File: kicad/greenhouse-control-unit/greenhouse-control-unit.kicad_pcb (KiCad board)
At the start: 2 copper layers, 71 parts, among them J1 Pluggable_Terminal_01x02, J10 Molex_KK-254_01x10, J10_LittleBuck1 Conn_01x01_Female, J11_LittleBuck1 Conn_01x01_Female, J12_BigBuck1 Conn_01x01_Female, J13_BigBuck1 Conn_01x01_Female, J14_LittleBuck1 Conn_01x01_Female, J15_LittleBuck1 Conn_01x01_Female, J2 Pluggable_Terminal_01x02, J3 Pluggable_Terminal_01x02, J4 Molex_KK-254_01x08, J5 Conn_01x10_Female, J6 Conn_01x10_Female, J6_BigBuck1 Conn_01x01_Female, J7 Conn_01x15_Female, J7_BigBuck1 Conn_01x01_Female, J8 Conn_01x15_Female, J9 Molex_KK-396_01x16, Q1 2N7000, Q10 IRLB8721PBF, Q11 IRLB8721PBF, Q12 2N7000, Q13 2N7000, Q2 2N7000, Q3 2N7000, Q4 IRLB8721PBF, Q5 IRLB8721PBF, Q6 IRLB8721PBF, Q7 IRLB8721PBF, Q8 IRLB8721PBF, Q9 IRLB8721PBF, U1 74HC595, U2 74HC595

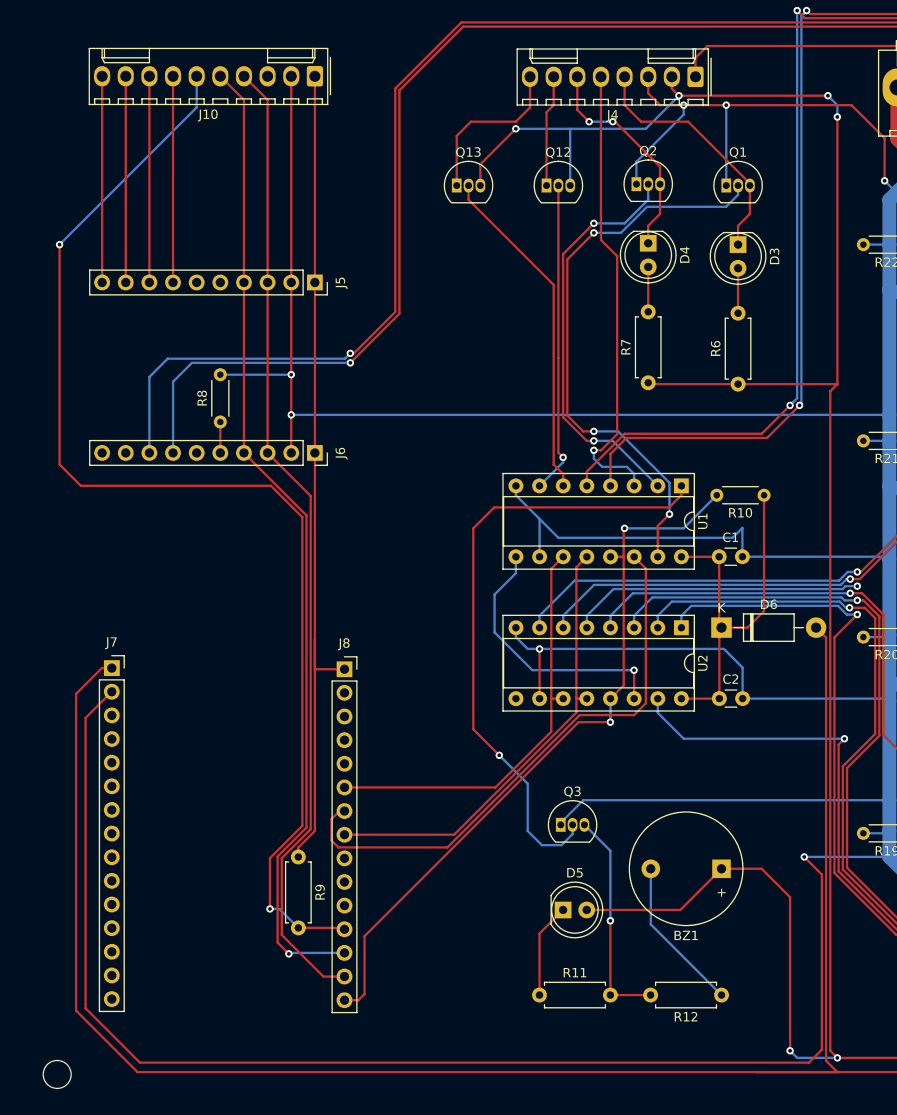
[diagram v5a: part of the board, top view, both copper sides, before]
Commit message: Tweaked PCB tracks
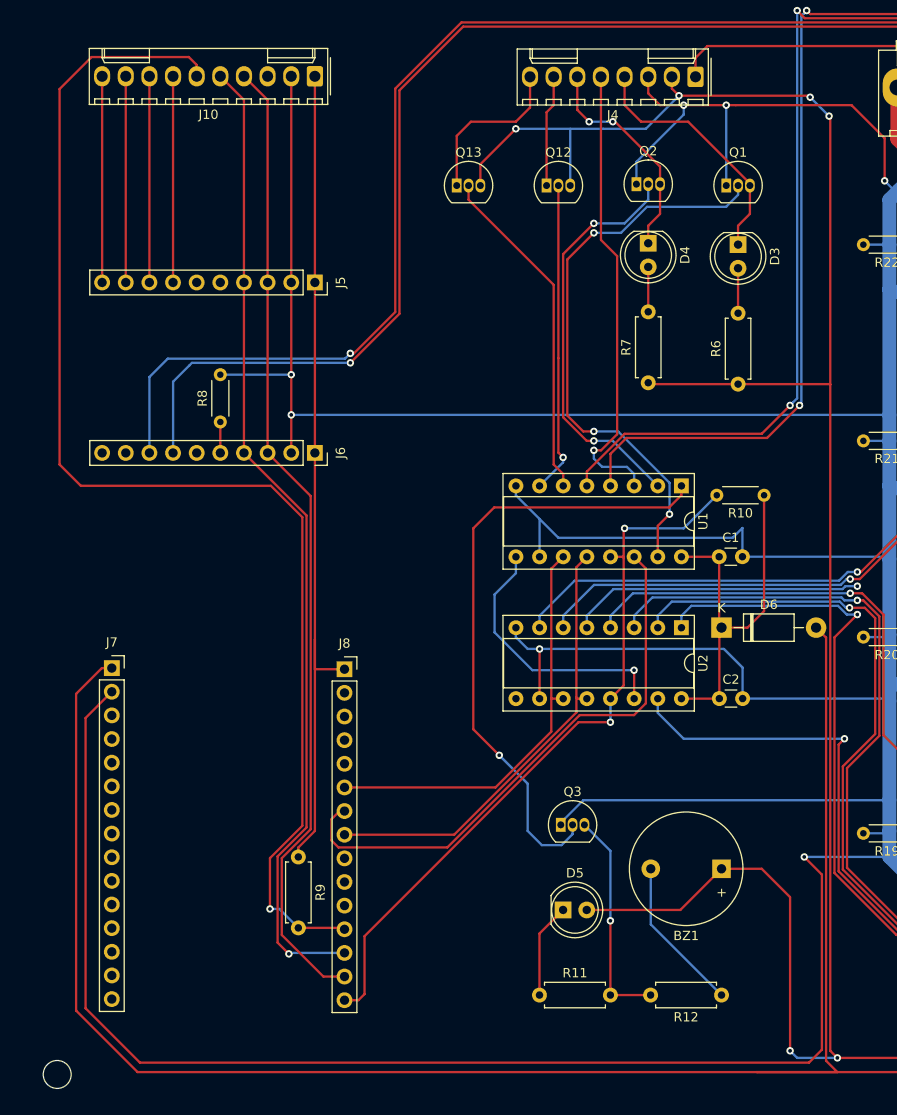
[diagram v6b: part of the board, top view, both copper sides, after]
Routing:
- net /MC_D3: track 128.7 -> 138.9 mm, vias 2 -> 1
- net +5V: track 372.0 -> 369.4 mm
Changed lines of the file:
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@@
     (fp_line (start 0.621 -0.92) (end 1.879 -0.92) (layer "F.SilkS") (width 0.12))
     (fp_line (start 0.621 0.92) (end 1.879 0.92) (layer "F.SilkS") (width 0.12))
+    (fp_line (start 3.55 1.05) (end 3.55 -1.05) (layer "F.CrtYd") (width 0.05))
     (fp_line (start -1.05 1.05) (end 3.55 1.05) (layer "F.CrtYd") (width 0.05))
     (fp_line (start -1.05 -1.05) (end -1.05 1.05) (layer "F.CrtYd") (width 0.05))
     (fp_line (start 3.55 -1.05) (end -1.05 -1.05) (layer "F.CrtYd") (width 0.05))
-    (fp_line (start 3.55 1.05) (end 3.55 -1.05) (layer "F.CrtYd") (width 0.05))
     (fp_line (start 2.75 -0.8) (end -0.25 -0.8) (layer "F.Fab") (width 0.1))
     (fp_line (start 2.75 0.8) (end 2.75 -0.8) (layer "F.Fab") (width 0.1))
@@
     (fp_line (start 5.08 0) (end 4.34 0) (layer "F.Fab") (width 0.1))
     (fp_line (start 0.74 -0.8) (end 0.74 0.8) (layer "F.Fab") (width 0.1))
+    (fp_line (start 4.34 -0.8) (end 0.74 -0.8) (layer "F.Fab") (width 0.1))
     (fp_line (start 0.74 0.8) (end 4.34 0.8) (layer "F.Fab") (width 0.1))
     (fp_line (start 4.34 0.8) (end 4.34 -0.8) (layer "F.Fab") (width 0.1))
-    (fp_line (start 4.34 -0.8) (end 0.74 -0.8) (layer "F.Fab") (width 0.1))
     (pad "1" thru_hole circle (at 0 0) (size 1.4 1.4) (drill 0.7) (layers *.Cu *.Mask)
       (net 37 "/SW0_SR_Q08") (pintype "passive"))
@@
   (segment (start 108.606642 128.872) (end 108.606642 134.84) (width 0.25) (layer "B.Cu") (net 2))
   (segment (start 108.606642 134.84) (end 116.206642 142.44) (width 0.25) (layer "B.Cu") (net 2))
-  (segment (start 127.890642 148.43) (end 127.890642 77.564) (width 0.25) (layer "F.Cu") (net 3))
-  (segment (start 128.652642 149.192) (end 127.890642 148.43) (width 0.25) (layer "F.Cu") (net 3))
-  (segment (start 127.890642 77.564) (end 128.652642 76.802) (width 0.25) (layer "F.Cu") (net 3))
+  (segment (start 125.73 45.974) (end 125.57 45.814) (width 0.25) (layer "F.Cu") (net 3))
   (segment (start 111.782642 133.296) (end 116.206642 128.872) (width 0.25) (layer "F.Cu") (net 3))
   (segment (start 90.298642 53.18) (end 94.108642 49.37) (width 0.25) (layer "F.Cu") (net 3))
   (segment (start 246.317642 110.013) (end 246.317642 103.01) (width 0.25) (layer "F.Cu") (net 3))
   (segment (start 117.984642 76.802) (end 108.480642 76.802) (width 0.25) (layer "F.Cu") (net 3))
+  (segment (start 127.890642 148.43) (end 128.652642 149.192) (width 0.25) (layer "F.Cu") (net 3))
   (segment (start 128.652642 149.192) (end 221.362642 149.192) (width 0.25) (layer "F.Cu") (net 3))
-  (segment (start 128.652642 76.802) (end 128.652642 48.1) (width 0.25) (layer "F.Cu") (net 3))
+  (segment (start 127.762 48.006) (end 127.890642 48.134642) (width 0.25) (layer "F.Cu") (net 3))
   (segment (start 221.362642 149.192) (end 226.188642 144.366) (width 0.25) (layer "F.Cu") (net 3))
   (segment (start 123.572642 131.92) (end 120.524642 128.872) (width 0.25) (layer "F.Cu") (net 3))
@@
   (segment (start 120.524642 128.872) (end 116.206642 128.872) (width 0.25) (layer "F.Cu") (net 3))
   (segment (start 226.188642 144.366) (end 226.188642 130.142) (width 0.25) (layer "F.Cu") (net 3))
+  (segment (start 117.984642 76.802) (end 127.856 76.802) (width 0.25) (layer "F.Cu") (net 3))
   (segment (start 110.872642 45.052) (end 110.872642 43.782) (width 0.25) (layer "F.Cu") (net 3))
+  (segment (start 125.57 45.814) (end 111.634642 45.814) (width 0.25) (layer "F.Cu") (net 3))
+  (segment (start 127.890642 48.134642) (end 127.890642 76.836642) (width 0.25) (layer "F.Cu") (net 3))
   (segment (start 226.188642 130.142) (end 246.317642 110.013) (width 0.25) (layer "F.Cu") (net 3))
+  (segment (start 127.856 76.802) (end 127.890642 76.836642) (width 0.25) (layer "F.Cu") (net 3))
   (segment (start 101.723642 133.296) (end 111.782642 133.296) (width 0.25) (layer "F.Cu") (net 3))
-  (segment (start 117.984642 76.802) (end 128.652642 76.802) (width 0.25) (layer "F.Cu") (net 3))
+  (segment (start 127.890642 76.836642) (end 127.890642 148.43) (width 0.25) (layer "F.Cu") (net 3))
   (segment (start 111.634642 45.814) (end 110.872642 45.052) (width 0.25) (layer "F.Cu") (net 3))
   (segment (start 90.298642 55.466) (end 90.298642 53.18) (width 0.25) (layer "F.Cu") (net 3))
   (segment (start 108.480642 76.802) (end 108.332642 76.654) (width 0.25) (layer "F.Cu") (net 3))
-  (segment (start 127.636642 45.814) (end 111.634642 45.814) (width 0.25) (layer "F.Cu") (net 3))
   (via (at 128.652642 149.192) (size 0.8) (drill 0.4) (layers "F.Cu" "B.Cu") (net 3))
   (via (at 123.572642 148.43) (size 0.8) (drill 0.4) (layers "F.Cu" "B.Cu") (net 3))
-  (via (at 127.636642 45.814) (size 0.8) (drill 0.4) (layers "F.Cu" "B.Cu") (net 3))
-  (via (at 128.652642 48.1) (size 0.8) (drill 0.4) (layers "F.Cu" "B.Cu") (net 3))
+  (via (at 125.73 45.974) (size 0.8) (drill 0.4) (layers "F.Cu" "B.Cu") (net 3))
+  (via (at 127.762 48.006) (size 0.8) (drill 0.4) (layers "F.Cu" "B.Cu") (net 3))
   (via (at 111.634642 45.814) (size 0.8) (drill 0.4) (layers "F.Cu" "B.Cu") (net 3))
   (via (at 94.108642 49.37) (size 0.8) (drill 0.4) (layers "F.Cu" "B.Cu") (net 3))
-  (segment (start 128.652642 46.83) (end 127.636642 45.814) (width 0.25) (layer "B.Cu") (net 3))
   (segment (start 103.506642 49.37) (end 108.078642 49.37) (width 0.25) (layer "B.Cu") (net 3))
   (segment (start 99.950642 49.37) (end 99.950642 55.466) (width 0.25) (layer "B.Cu") (net 3))
@@
   (segment (start 103.506642 49.37) (end 94.108642 49.37) (width 0.25) (layer "B.Cu") (net 3))
   (segment (start 124.334642 149.192) (end 128.652642 149.192) (width 0.25) (layer "B.Cu") (net 3))
-  (segment (start 128.652642 48.1) (end 128.652642 46.83) (width 0.25) (layer "B.Cu") (net 3))
+  (segment (start 125.73 45.974) (end 127.762 48.006) (width 0.25) (layer "B.Cu") (net 3))
   (segment (start 120.016642 150.716) (end 224.791642 150.716) (width 0.25) (layer "F.Cu") (net 4))
   (segment (start 127.441122 149.50448) (end 127.441122 104.03848) (width 0.25) (layer "F.Cu") (net 4))
@@
   (segment (start 74.296642 123.5525) (end 74.296642 125.824) (width 0.25) (layer "F.Cu") (net 46))
   (segment (start 75.699642 122.672) (end 75.177142 122.672) (width 0.25) (layer "F.Cu") (net 46))
-  (segment (start 71.170082 124.249406) (end 71.170082 91.100158) (width 0.25) (layer "F.Cu") (net 47))
+  (segment (start 58.973321 41.656) (end 59.818642 42.501321) (width 0.25) (layer "F.Cu") (net 47))
   (segment (start 67.793924 87.724) (end 47.372642 87.724) (width 0.25) (layer "F.Cu") (net 47))
-  (segment (start 47.372642 87.724) (end 45.086642 85.438) (width 0.25) (layer "F.Cu") (net 47))
+  (segment (start 71.170082 91.100158) (end 67.793924 87.724) (width 0.25) (layer "F.Cu") (net 47))
   (segment (start 67.692642 133.19) (end 67.692642 127.726846) (width 0.25) (layer "F.Cu") (net 47))
+  (segment (start 45.086642 45.098526) (end 48.529168 41.656) (width 0.25) (layer "F.Cu") (net 47))
   (segment (start 67.692642 127.726846) (end 71.170082 124.249406) (width 0.25) (layer "F.Cu") (net 47))
+  (segment (start 47.372642 87.724) (end 45.086642 85.438) (width 0.25) (layer "F.Cu") (net 47))
+  (segment (start 45.086642 85.438) (end 45.086642 45.098526) (width 0.25) (layer "F.Cu") (net 47))
   (segment (start 75.549642 135.222) (end 75.699642 135.372) (width 0.25) (layer "F.Cu") (net 47))
-  (segment (start 71.170082 91.100158) (end 67.793924 87.724) (width 0.25) (layer "F.Cu") (net 47))
-  (segment (start 45.086642 85.438) (end 45.086642 61.816) (width 0.25) (layer "F.Cu") (net 47))
+  (segment (start 59.818642 42.501321) (end 59.818642 43.726) (width 0.25) (layer "F.Cu") (net 47))
+  (segment (start 48.529168 41.656) (end 58.973321 41.656) (width 0.25) (layer "F.Cu") (net 47))
+  (segment (start 71.170082 124.249406) (end 71.170082 91.100158) (width 0.25) (layer "F.Cu") (net 47))
   (segment (start 70.740642 135.222) (end 75.549642 135.222) (width 0.25) (layer "F.Cu") (net 47))
-  (via (at 45.086642 61.816) (size 0.8) (drill 0.4) (layers "F.Cu" "B.Cu") (net 47))
   (via (at 67.692642 133.19) (size 0.8) (drill 0.4) (layers "F.Cu" "B.Cu") (net 47))
   (segment (start 68.708642 133.19) (end 70.740642 135.222) (width 0.25) (layer "B.Cu") (net 47))
-  (segment (start 59.818642 47.084) (end 59.818642 43.726) (width 0.25) (layer "B.Cu") (net 47))
-  (segment (start 45.086642 61.816) (end 59.818642 47.084) (width 0.25) (layer "B.Cu") (net 47))
   (segment (start 67.692642 133.19) (end 68.708642 133.19) (width 0.25) (layer "B.Cu") (net 47))
   (segment (start 62.358642 84.193) (end 62.358642 80.866) (width 0.25) (layer "F.Cu") (net 48))

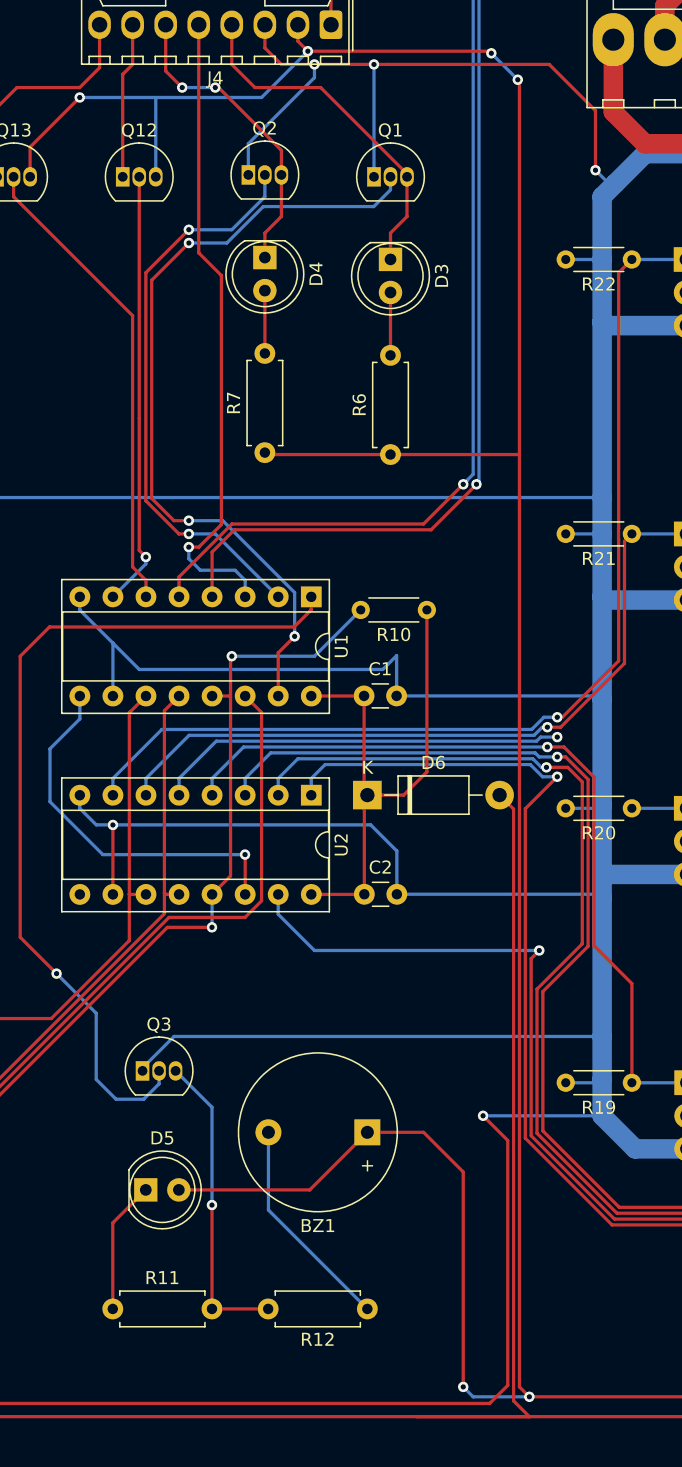
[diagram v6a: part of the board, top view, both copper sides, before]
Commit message: Tweaked PCB tracks (more)
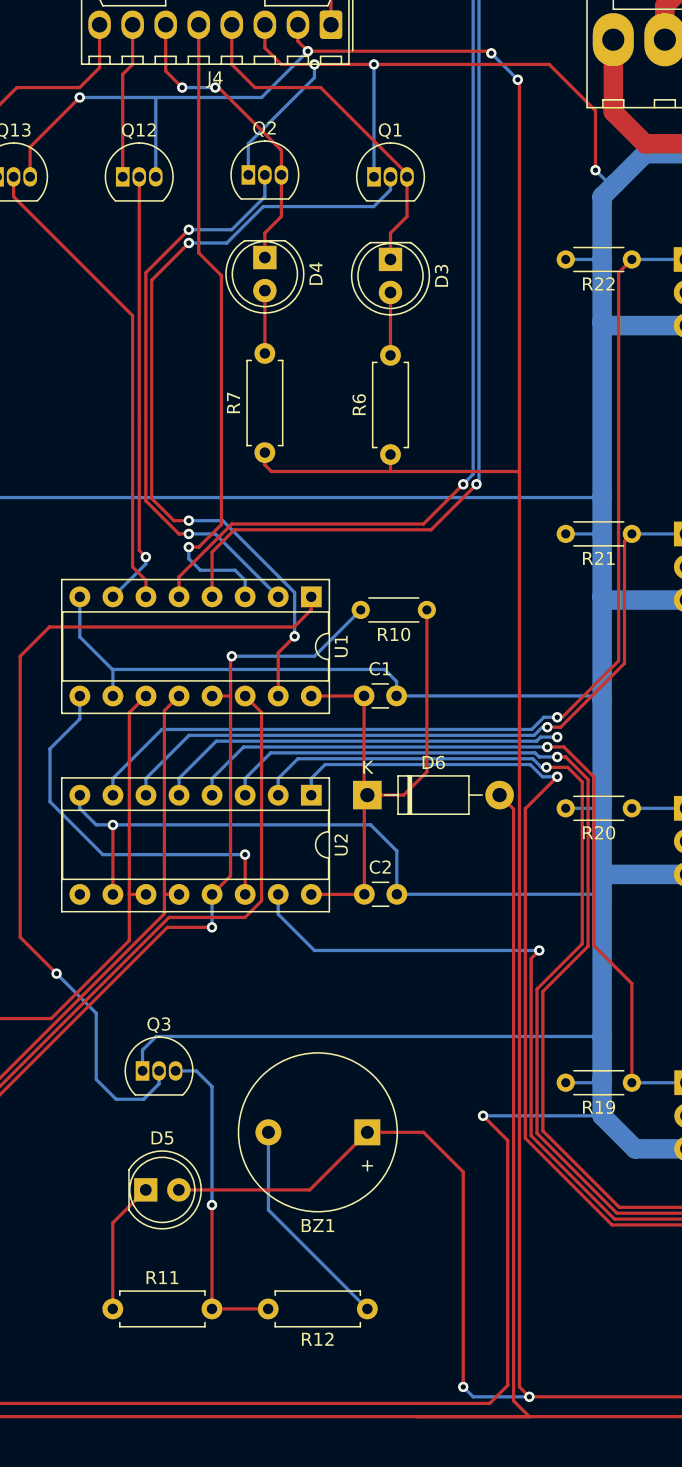
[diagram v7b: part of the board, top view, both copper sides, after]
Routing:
- net +5V: track 369.4 -> 372.3 mm
- net GND: track 932.8 -> 930.8 mm
- net Net-(Q3-Pad3): track 23.8 -> 24.7 mm

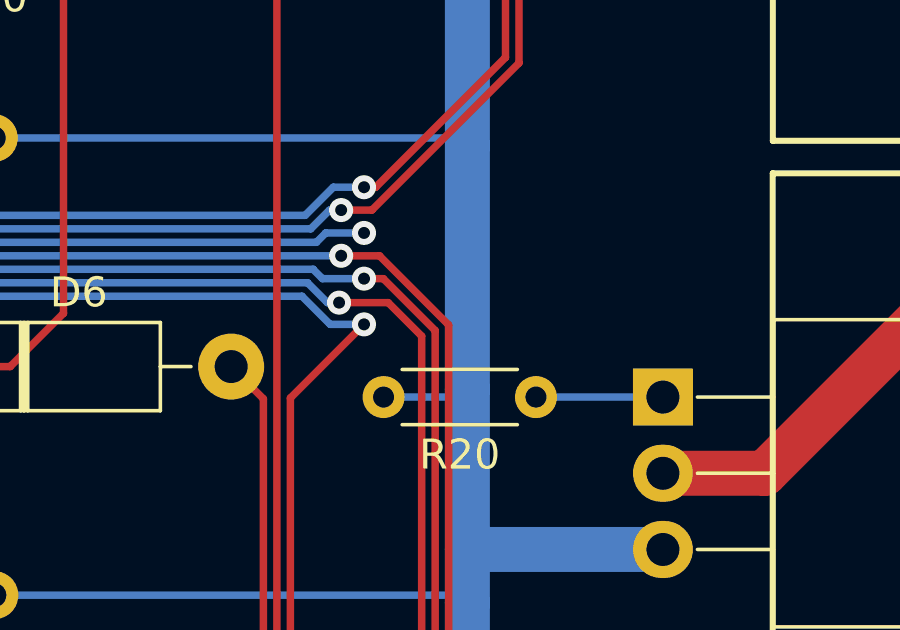
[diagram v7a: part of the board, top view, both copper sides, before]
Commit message: Add missing trace for Q9
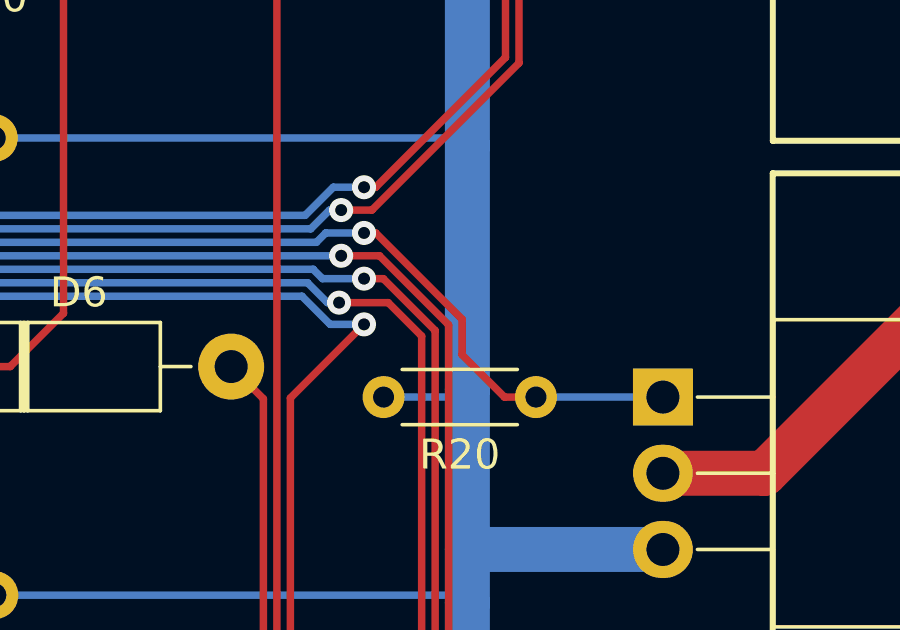
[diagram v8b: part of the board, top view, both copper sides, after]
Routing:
- net /SW5_SR_Q13: track 35.9 -> 44.6 mm
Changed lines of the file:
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@@
   (segment (start 104.278642 102.974) (end 104.278642 101.704) (width 0.25) (layer "B.Cu") (net 42))
   (segment (start 104.278642 101.704) (end 104.268642 101.694) (width 0.25) (layer "B.Cu") (net 42))
+  (segment (start 134.065202 101.389409) (end 134.065202 102.569202) (width 0.25) (layer "F.Cu") (net 43))
+  (segment (start 131.184753 98.50896) (end 134.065202 101.389409) (width 0.25) (layer "F.Cu") (net 43))
+  (segment (start 134.065202 102.569202) (end 135.476 103.98) (width 0.25) (layer "F.Cu") (net 43))
+  (segment (start 135.476 103.98) (end 136.526642 103.98) (width 0.25) (layer "F.Cu") (net 43))
+  (segment (start 130.795658 98.50896) (end 131.184753 98.50896) (width 0.25) (layer "F.Cu") (net 43))
   (via (at 130.795658 98.50896) (size 0.8) (drill 0.4) (layers "F.Cu" "B.Cu") (net 43))
   (segment (start 101.738642 102.974) (end 101.738642 101.704) (width 0.25) (layer "B.Cu") (net 43))
